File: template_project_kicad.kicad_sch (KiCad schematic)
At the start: 1 part

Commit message: First draft of pcb
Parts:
- added D1, D2: LED, LED_THT:LED_D3.0mm, symbol Device:LED
- added J1: Conn_01x04_Pin, Connector_PinSocket_2.54mm:PinSocket_1x04_P2.54mm_Vertical, symbol Connector:Conn_01x04_Pin
- added R1, R2: 150, Resistor_THT:R_Axial_DIN0204_L3.6mm_D1.6mm_P5.08mm_Horizontal, symbol Device:R
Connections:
- net GND: now reaches A1.13 (GND)
- net GND: now also A1.18 (GND), A1.23 (GND), A1.28 (GND), A1.3 (GND), A1.33 (GND|AGND), A1.38 (GND), A1.8 (GND), D1.1 (K), D2.1 (K), J1.2 (Pin_2), J1.4 (Pin_4)
- net at A1.26 (I2C0_SDA|GP20): now also J1.1 (Pin_1)
- net at A1.27 (I2C0_SCL|GP21): now also J1.3 (Pin_3)
- net LED1: now reaches A1.4 (GP2|SPI0_SCK|I2C1_SDA)
- net LED1: now also R1.2
- net LED2: now reaches A1.9 (GP6|SPI0_SCK|I2C1_SDA)
- net LED2: now also R2.2
- new net: D2.2 (A), R2.1
- new net: D1.2 (A), R1.1
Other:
- note added: "GP20"
- note added: "GP21"
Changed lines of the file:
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@@
 (kicad_sch (version 20230121) (generator eeschema)
   (paper "A4")
+  (wire (pts (xy 93.98 85.09) (xy 100.33 85.09))
+    (stroke (width 0) (type default))
+  )
+  (wire (pts (xy 92.71 62.23) (xy 100.33 62.23))
+    (stroke (width 0) (type default))
+  )
+  (wire (pts (xy 241.3 87.63) (xy 241.3 74.93))
+    (stroke (width 0) (type default))
+  )
+  (wire (pts (xy 44.45 62.23) (xy 41.91 62.23))
+    (stroke (width 0) (type default))
+  )
+  (wire (pts (xy 180.34 87.63) (xy 241.3 87.63))
+    (stroke (width 0) (type default))
+  )
+  (wire (pts (xy 93.98 72.39) (xy 100.33 72.39))
+    (stroke (width 0) (type default))
+  )
+  (wire (pts (xy 231.14 72.39) (xy 242.57 72.39))
+    (stroke (width 0) (type default))
+  )
+  (wire (pts (xy 93.98 97.79) (xy 100.33 97.79))
+    (stroke (width 0) (type default))
+  )
+  (wire (pts (xy 231.14 77.47) (xy 242.57 77.47))
+    (stroke (width 0) (type default))
+  )
+  (wire (pts (xy 180.34 59.69) (xy 184.15 59.69))
+    (stroke (width 0) (type default))
+  )
+  (wire (pts (xy 180.34 97.79) (xy 184.15 97.79))
+    (stroke (width 0) (type default))
+  )
+  (wire (pts (xy 180.34 85.09) (xy 184.15 85.09))
+    (stroke (width 0) (type default))
+  )
+  (wire (pts (xy 180.34 90.17) (xy 242.57 90.17))
+    (stroke (width 0) (type default))
+  )
+  (wire (pts (xy 180.34 72.39) (xy 184.15 72.39))
+    (stroke (width 0) (type default))
+  )
+  (wire (pts (xy 241.3 74.93) (xy 242.57 74.93))
+    (stroke (width 0) (type default))
+  )
+  (wire (pts (xy 44.45 74.93) (xy 41.91 74.93))
+    (stroke (width 0) (type default))
+  )
+  (wire (pts (xy 93.98 59.69) (xy 100.33 59.69))
+    (stroke (width 0) (type default))
+  )
+  (wire (pts (xy 92.71 74.93) (xy 100.33 74.93))
+    (stroke (width 0) (type default))
+  )
+  (wire (pts (xy 242.57 90.17) (xy 242.57 80.01))
+    (stroke (width 0) (type default))
+  )
+  (text "GP20" (at 234.95 81.28 0)
+    (effects (font (size 1.27 1.27)) (justify left bottom))
+  )
+  (text "GP21" (at 234.95 76.2 0)
+    (effects (font (size 1.27 1.27)) (justify left bottom))
+  )
+  (label "GND" (at 41.91 62.23 180) (fields_autoplaced)
+    (effects (font (size 1.27 1.27)) (justify right bottom))
+  )
+  (label "GND" (at 93.98 72.39 0) (fields_autoplaced)
+    (effects (font (size 1.27 1.27)) (justify left bottom))
+  )
+  (label "GND" (at 184.15 85.09 0) (fields_autoplaced)
+    (effects (font (size 1.27 1.27)) (justify left bottom))
+  )
+  (label "GND" (at 184.15 97.79 0) (fields_autoplaced)
+    (effects (font (size 1.27 1.27)) (justify left bottom))
+  )
+  (label "GND" (at 93.98 59.69 0) (fields_autoplaced)
+    (effects (font (size 1.27 1.27)) (justify left bottom))
+  )
+  (label "LED1" (at 92.71 62.23 180) (fields_autoplaced)
+    (effects (font (size 1.27 1.27)) (justify right bottom))
+  )
+  (label "GND" (at 184.15 59.69 0) (fields_autoplaced)
+    (effects (font (size 1.27 1.27)) (justify left bottom))
+  )
+  (label "LED2" (at 59.69 74.93 0) (fields_autoplaced)
+    (effects (font (size 1.27 1.27)) (justify left bottom))
+  )
+  (label "GND" (at 41.91 74.93 180) (fields_autoplaced)
+    (effects (font (size 1.27 1.27)) (justify right bottom))
+  )
+  (label "GND" (at 93.98 85.09 0) (fields_autoplaced)
+    (effects (font (size 1.27 1.27)) (justify left bottom))
+  )
+  (label "GND" (at 231.14 77.47 180) (fields_autoplaced)
+    (effects (font (size 1.27 1.27)) (justify right bottom))
+  )
+  (label "GND" (at 184.15 72.39 0) (fields_autoplaced)
+    (effects (font (size 1.27 1.27)) (justify left bottom))
+  )
+  (label "GND" (at 231.14 72.39 180) (fields_autoplaced)
+    (effects (font (size 1.27 1.27)) (justify right bottom))
+  )
+  (label "LED1" (at 59.69 62.23 0) (fields_autoplaced)
+    (effects (font (size 1.27 1.27)) (justify left bottom))
+  )
+  (label "GND" (at 93.98 97.79 0) (fields_autoplaced)
+    (effects (font (size 1.27 1.27)) (justify left bottom))
+  )
+  (label "LED2" (at 92.71 74.93 180) (fields_autoplaced)
+    (effects (font (size 1.27 1.27)) (justify right bottom))
+  )
   (symbol (lib_id "twyleg-board-connectors:RaspberryPi-Pico") (at 139.7 52.07 0) (unit 1)
     (in_bom yes) (on_board yes) (dnp no) (fields_autoplaced)
@@
         )
       )
+    )
+  )
+  (symbol (lib_id "Device:LED") (at 48.26 74.93 0) (unit 1)
+    (in_bom yes) (on_board yes) (dnp no)
+    (property "Reference" "D2" (at 48.26 69.85 0)
+      (effects (font (size 1.27 1.27)) (justify right))
+    )
+    (property "Value" "LED" (at 48.26 72.39 0)
+      (effects (font (size 1.27 1.27)) (justify right))
+    )
+    (property "Footprint" "LED_THT:LED_D3.0mm" (at 48.26 74.93 0)
+      (effects (font (size 1.27 1.27)) hide)
+    )
+    (property "Datasheet" "~" (at 48.26 74.93 0)
+      (effects (font (size 1.27 1.27)) hide)
+    )
+    (pin "1")
+    (pin "2")
+    (instances
+      (project "template_project_kicad"
+        (path "/b464f893-b088-4709-8572-04b2e8773c63"
+          (reference "D2") (unit 1)
+        )
+      )
+    )
+  )
+  (symbol (lib_id "Connector:Conn_01x04_Pin") (at 247.65 77.47 180) (unit 1)
+    (in_bom yes) (on_board yes) (dnp no) (fields_autoplaced)
+    (property "Reference" "J1" (at 248.92 74.93 0)
+      (effects (font (size 1.27 1.27)) (justify right))
+    )
+    (property "Value" "Conn_01x04_Pin" (at 248.92 77.47 0)
+      (effects (font (size 1.27 1.27)) (justify right))
+    )
+    (property "Footprint" "Connector_PinSocket_2.54mm:PinSocket_1x04_P2.54mm_Vertical" (at 247.65 77.47 0)
+      (effects (font (size 1.27 1.27)) hide)
+    )
+    (property "Datasheet" "~" (at 247.65 77.47 0)
+      (effects (font (size 1.27 1.27)) hide)
+    )
+    (pin "4")
+    (pin "3")
+    (pin "2")
+    (pin "1")
+    (instances
+      (project "template_project_kicad"
+        (path "/b464f893-b088-4709-8572-04b2e8773c63"
+          (reference "J1") (unit 1)
+        )
+      )
+    )
+  )
+  (symbol (lib_id "Device:R") (at 55.88 62.23 90) (unit 1)
+    (in_bom yes) (on_board yes) (dnp no) (fields_autoplaced)
+    (property "Reference" "R1" (at 55.88 55.88 90)
+      (effects (font (size 1.27 1.27)))
+    )
+    (property "Value" "150" (at 55.88 58.42 90)
+      (effects (font (size 1.27 1.27)))
+    )
+    (property "Footprint" "Resistor_THT:R_Axial_DIN0204_L3.6mm_D1.6mm_P5.08mm_Horizontal" (at 55.88 64.008 90)
+      (effects (font (size 1.27 1.27)) hide)
+    )
+    (property "Datasheet" "~" (at 55.88 62.23 0)
+      (effects (font (size 1.27 1.27)) hide)
+    )
+    (pin "1")
+    (pin "2")
+    (instances
+      (project "template_project_kicad"
+        (path "/b464f893-b088-4709-8572-04b2e8773c63"
+          (reference "R1") (unit 1)
+        )
+      )
+    )
+  )
+  (symbol (lib_id "Device:R") (at 55.88 74.93 90) (unit 1)
+    (in_bom yes) (on_board yes) (dnp no) (fields_autoplaced)
+    (property "Reference" "R2" (at 55.88 68.58 90)
+      (effects (font (size 1.27 1.27)))
+    )
+    (property "Value" "150" (at 55.88 71.12 90)
+      (effects (font (size 1.27 1.27)))
+    )
+    (property "Footprint" "Resistor_THT:R_Axial_DIN0204_L3.6mm_D1.6mm_P5.08mm_Horizontal" (at 55.88 76.708 90)
+      (effects (font (size 1.27 1.27)) hide)
+    )
+    (property "Datasheet" "~" (at 55.88 74.93 0)
+      (effects (font (size 1.27 1.27)) hide)
+    )
+    (pin "1")
+    (pin "2")
+    (instances
+      (project "template_project_kicad"
+        (path "/b464f893-b088-4709-8572-04b2e8773c63"
+          (reference "R2") (unit 1)
+        )
+      )
+    )
+  )
+  (symbol (lib_id "Device:LED") (at 48.26 62.23 0) (unit 1)
+    (in_bom yes) (on_board yes) (dnp no) (fields_autoplaced)
+    (property "Reference" "D1" (at 46.6725 55.88 0)
+      (effects (font (size 1.27 1.27)))
+    )
+    (property "Value" "LED" (at 46.6725 58.42 0)
+      (effects (font (size 1.27 1.27)))
+    )
+    (property "Footprint" "LED_THT:LED_D3.0mm" (at 48.26 62.23 0)
+      (effects (font (size 1.27 1.27)) hide)
+    )
+    (property "Datasheet" "~" (at 48.26 62.23 0)
+      (effects (font (size 1.27 1.27)) hide)
+    )
+    (pin "2")
+    (pin "1")
+    (instances
+      (project "template_project_kicad"
+        (path "/b464f893-b088-4709-8572-04b2e8773c63"
+          (reference "D1") (unit 1)
+        )
+      )

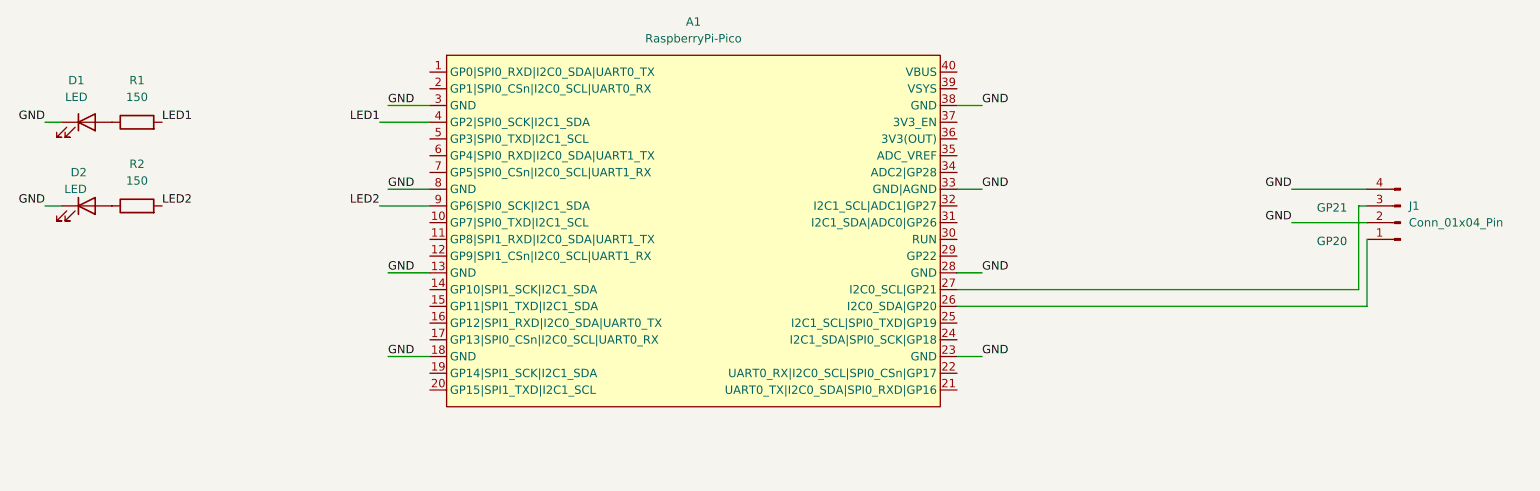
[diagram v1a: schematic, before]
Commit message: Updated RPI PicoW footprint and minor improvements
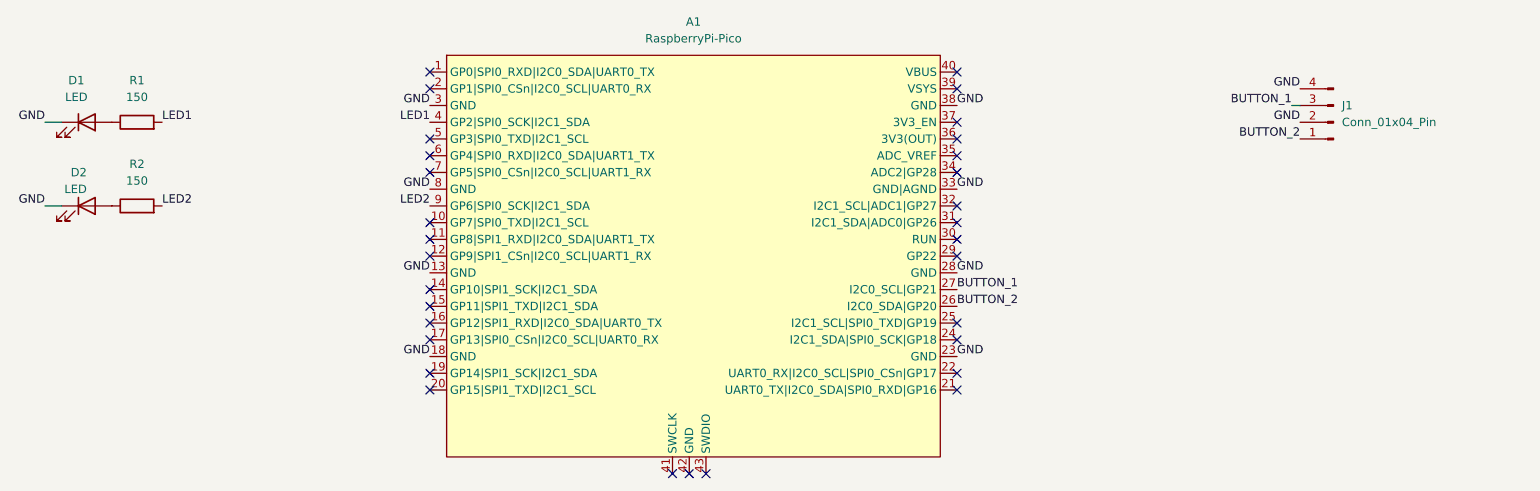
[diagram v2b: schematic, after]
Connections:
- net BUTTON_2: now reaches A1.26 (I2C0_SDA|GP20), J1.1 (Pin_1)
- net BUTTON_1: now reaches A1.27 (I2C0_SCL|GP21), J1.3 (Pin_3)
- no-connect marks 0 -> 31
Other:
- note removed: "GP20"
- note removed: "GP21"
- moved on the sheet: J1
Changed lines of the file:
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@@
 (kicad_sch (version 20230121) (generator eeschema)
   (paper "A4")
-  (wire (pts (xy 93.98 85.09) (xy 100.33 85.09))
-    (stroke (width 0) (type default))
-  )
-  (wire (pts (xy 92.71 62.23) (xy 100.33 62.23))
-    (stroke (width 0) (type default))
-  )
-  (wire (pts (xy 241.3 87.63) (xy 241.3 74.93))
-    (stroke (width 0) (type default))
-  )
+  (no_connect (at 100.33 100.33))
+  (no_connect (at 142.24 115.57))
+  (no_connect (at 180.34 82.55))
+  (no_connect (at 180.34 92.71))
+  (no_connect (at 180.34 77.47))
+  (no_connect (at 180.34 62.23))
+  (no_connect (at 139.7 115.57))
+  (no_connect (at 137.16 115.57))
+  (no_connect (at 100.33 102.87))
+  (no_connect (at 180.34 64.77))
+  (no_connect (at 100.33 69.85))
+  (no_connect (at 100.33 64.77))
+  (no_connect (at 180.34 102.87))
+  (no_connect (at 180.34 80.01))
+  (no_connect (at 100.33 80.01))
+  (no_connect (at 100.33 87.63))
+  (no_connect (at 180.34 100.33))
+  (no_connect (at 180.34 67.31))
+  (no_connect (at 180.34 95.25))
+  (no_connect (at 180.34 57.15))
+  (no_connect (at 100.33 67.31))
+  (no_connect (at 100.33 77.47))
+  (no_connect (at 100.33 57.15))
+  (no_connect (at 100.33 82.55))
+  (no_connect (at 180.34 54.61))
+  (no_connect (at 180.34 74.93))
+  (no_connect (at 100.33 95.25))
+  (no_connect (at 180.34 69.85))
+  (no_connect (at 100.33 92.71))
+  (no_connect (at 100.33 90.17))
+  (no_connect (at 100.33 54.61))
   (wire (pts (xy 44.45 62.23) (xy 41.91 62.23))
     (stroke (width 0) (type default))
   )
-  (wire (pts (xy 180.34 87.63) (xy 241.3 87.63))
-    (stroke (width 0) (type default))
-  )
-  (wire (pts (xy 93.98 72.39) (xy 100.33 72.39))
-    (stroke (width 0) (type default))
-  )
-  (wire (pts (xy 231.14 72.39) (xy 242.57 72.39))
-    (stroke (width 0) (type default))
-  )
-  (wire (pts (xy 93.98 97.79) (xy 100.33 97.79))
-    (stroke (width 0) (type default))
-  )
-  (wire (pts (xy 231.14 77.47) (xy 242.57 77.47))
-    (stroke (width 0) (type default))
-  )
-  (wire (pts (xy 180.34 59.69) (xy 184.15 59.69))
-    (stroke (width 0) (type default))
-  )
-  (wire (pts (xy 180.34 97.79) (xy 184.15 97.79))
-    (stroke (width 0) (type default))
-  )
-  (wire (pts (xy 180.34 85.09) (xy 184.15 85.09))
-    (stroke (width 0) (type default))
-  )
-  (wire (pts (xy 180.34 90.17) (xy 242.57 90.17))
-    (stroke (width 0) (type default))
-  )
-  (wire (pts (xy 180.34 72.39) (xy 184.15 72.39))
-    (stroke (width 0) (type default))
-  )
-  (wire (pts (xy 241.3 74.93) (xy 242.57 74.93))
+  (wire (pts (xy 231.14 59.69) (xy 232.41 59.69))
     (stroke (width 0) (type default))
   )
@@
     (stroke (width 0) (type default))
   )
-  (wire (pts (xy 93.98 59.69) (xy 100.33 59.69))
-    (stroke (width 0) (type default))
-  )
-  (wire (pts (xy 92.71 74.93) (xy 100.33 74.93))
-    (stroke (width 0) (type default))
-  )
-  (wire (pts (xy 242.57 90.17) (xy 242.57 80.01))
-    (stroke (width 0) (type default))
-  )
-  (text "GP20" (at 234.95 81.28 0)
-    (effects (font (size 1.27 1.27)) (justify left bottom))
-  )
-  (text "GP21" (at 234.95 76.2 0)
+  (label "BUTTON_2" (at 232.41 64.77 180) (fields_autoplaced)
+    (effects (font (size 1.27 1.27)) (justify right bottom))
+  )
+  (label "BUTTON_2" (at 180.34 90.17 0) (fields_autoplaced)
     (effects (font (size 1.27 1.27)) (justify left bottom))
   )
@@
     (effects (font (size 1.27 1.27)) (justify right bottom))
   )
-  (label "GND" (at 93.98 72.39 0) (fields_autoplaced)
-    (effects (font (size 1.27 1.27)) (justify left bottom))
-  )
-  (label "GND" (at 184.15 85.09 0) (fields_autoplaced)
-    (effects (font (size 1.27 1.27)) (justify left bottom))
-  )
-  (label "GND" (at 184.15 97.79 0) (fields_autoplaced)
-    (effects (font (size 1.27 1.27)) (justify left bottom))
-  )
-  (label "GND" (at 93.98 59.69 0) (fields_autoplaced)
-    (effects (font (size 1.27 1.27)) (justify left bottom))
-  )
-  (label "LED1" (at 92.71 62.23 180) (fields_autoplaced)
-    (effects (font (size 1.27 1.27)) (justify right bottom))
-  )
-  (label "GND" (at 184.15 59.69 0) (fields_autoplaced)
+  (label "BUTTON_1" (at 231.14 59.69 180) (fields_autoplaced)
+    (effects (font (size 1.27 1.27)) (justify right bottom))
+  )
+  (label "GND" (at 100.33 72.39 180) (fields_autoplaced)
+    (effects (font (size 1.27 1.27)) (justify right bottom))
+  )
+  (label "GND" (at 180.34 85.09 0) (fields_autoplaced)
+    (effects (font (size 1.27 1.27)) (justify left bottom))
+  )
+  (label "GND" (at 180.34 97.79 0) (fields_autoplaced)
+    (effects (font (size 1.27 1.27)) (justify left bottom))
+  )
+  (label "GND" (at 100.33 59.69 180) (fields_autoplaced)
+    (effects (font (size 1.27 1.27)) (justify right bottom))
+  )
+  (label "LED1" (at 100.33 62.23 180) (fields_autoplaced)
+    (effects (font (size 1.27 1.27)) (justify right bottom))
+  )
+  (label "GND" (at 180.34 59.69 0) (fields_autoplaced)
     (effects (font (size 1.27 1.27)) (justify left bottom))
   )
@@
     (effects (font (size 1.27 1.27)) (justify right bottom))
   )
-  (label "GND" (at 93.98 85.09 0) (fields_autoplaced)
-    (effects (font (size 1.27 1.27)) (justify left bottom))
-  )
-  (label "GND" (at 231.14 77.47 180) (fields_autoplaced)
-    (effects (font (size 1.27 1.27)) (justify right bottom))
-  )
-  (label "GND" (at 184.15 72.39 0) (fields_autoplaced)
-    (effects (font (size 1.27 1.27)) (justify left bottom))
-  )
-  (label "GND" (at 231.14 72.39 180) (fields_autoplaced)
+  (label "GND" (at 100.33 85.09 180) (fields_autoplaced)
+    (effects (font (size 1.27 1.27)) (justify right bottom))
+  )
+  (label "GND" (at 232.41 62.23 180) (fields_autoplaced)
+    (effects (font (size 1.27 1.27)) (justify right bottom))
+  )
+  (label "GND" (at 180.34 72.39 0) (fields_autoplaced)
+    (effects (font (size 1.27 1.27)) (justify left bottom))
+  )
+  (label "GND" (at 232.41 57.15 180) (fields_autoplaced)
     (effects (font (size 1.27 1.27)) (justify right bottom))
   )
@@
     (effects (font (size 1.27 1.27)) (justify left bottom))
   )
-  (label "GND" (at 93.98 97.79 0) (fields_autoplaced)
-    (effects (font (size 1.27 1.27)) (justify left bottom))
-  )
-  (label "LED2" (at 92.71 74.93 180) (fields_autoplaced)
-    (effects (font (size 1.27 1.27)) (justify right bottom))
+  (label "GND" (at 100.33 97.79 180) (fields_autoplaced)
+    (effects (font (size 1.27 1.27)) (justify right bottom))
+  )
+  (label "LED2" (at 100.33 74.93 180) (fields_autoplaced)
+    (effects (font (size 1.27 1.27)) (justify right bottom))
+  )
+  (label "BUTTON_1" (at 180.34 87.63 0) (fields_autoplaced)
+    (effects (font (size 1.27 1.27)) (justify left bottom))
   )
   (symbol (lib_id "twyleg-board-connectors:RaspberryPi-Pico") (at 139.7 52.07 0) (unit 1)
@@
     (pin "30")
     (pin "5")
+    (pin "42")
+    (pin "43")
+    (pin "41")
     (instances
       (project "template_project_kicad"
@@
     )
   )
-  (symbol (lib_id "Connector:Conn_01x04_Pin") (at 247.65 77.47 180) (unit 1)
+  (symbol (lib_id "Connector:Conn_01x04_Pin") (at 237.49 62.23 180) (unit 1)
     (in_bom yes) (on_board yes) (dnp no) (fields_autoplaced)
-    (property "Reference" "J1" (at 248.92 74.93 0)
-      (effects (font (size 1.27 1.27)) (justify right))
-    )
-    (property "Value" "Conn_01x04_Pin" (at 248.92 77.47 0)
-      (effects (font (size 1.27 1.27)) (justify right))
-    )
-    (property "Footprint" "Connector_PinSocket_2.54mm:PinSocket_1x04_P2.54mm_Vertical" (at 247.65 77.47 0)
-      (effects (font (size 1.27 1.27)) hide)
-    )
-    (property "Datasheet" "~" (at 247.65 77.47 0)
-      (effects (font (size 1.27 1.27)) hide)
-    )
+    (property "Reference" "J1" (at 238.76 59.69 0)
+      (effects (font (size 1.27 1.27)) (justify right))
+    )
+    (property "Value" "Conn_01x04_Pin" (at 238.76 62.23 0)
+      (effects (font (size 1.27 1.27)) (justify right))
+    )
+    (property "Footprint" "Connector_PinSocket_2.54mm:PinSocket_1x04_P2.54mm_Vertical" (at 237.49 62.23 0)
+      (effects (font (size 1.27 1.27)) hide)
+    )
+    (property "Datasheet" "~" (at 237.49 62.23 0)
+      (effects (font (size 1.27 1.27)) hide)
+    )
